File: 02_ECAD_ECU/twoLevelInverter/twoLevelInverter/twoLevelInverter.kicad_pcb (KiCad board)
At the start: 2 copper layers, 88.9 x 115.3 mm, 72 parts, among them IC1 MP9486AGN-Z, IC2 INA240A4DR, IC3 BTN8982TAAUMA1, IC4 INA240A4DR, IC5 BTN8982TAAUMA1, IC6 INA240A4DR, IC7 BTN8982TAAUMA1, J1 FX10A-80S_8-SV_71_, J2 43045-0812, J3 Screw_Terminal_01x04, J4 Screw_Terminal_01x04, J5 Screw_Terminal_01x02, J6 Screw_Terminal_01x02, J7 Screw_Terminal_01x02, U1 290mA, U10 30k, U11 2.4k, U12 22u, U13 15u, U14 RED, U15 1k, U2 100k, U3 68k, U4 MP2303ADN-LF, U5 10nF, U6 100nF, U7 3.3nF, U8 5.6k, U9 10k

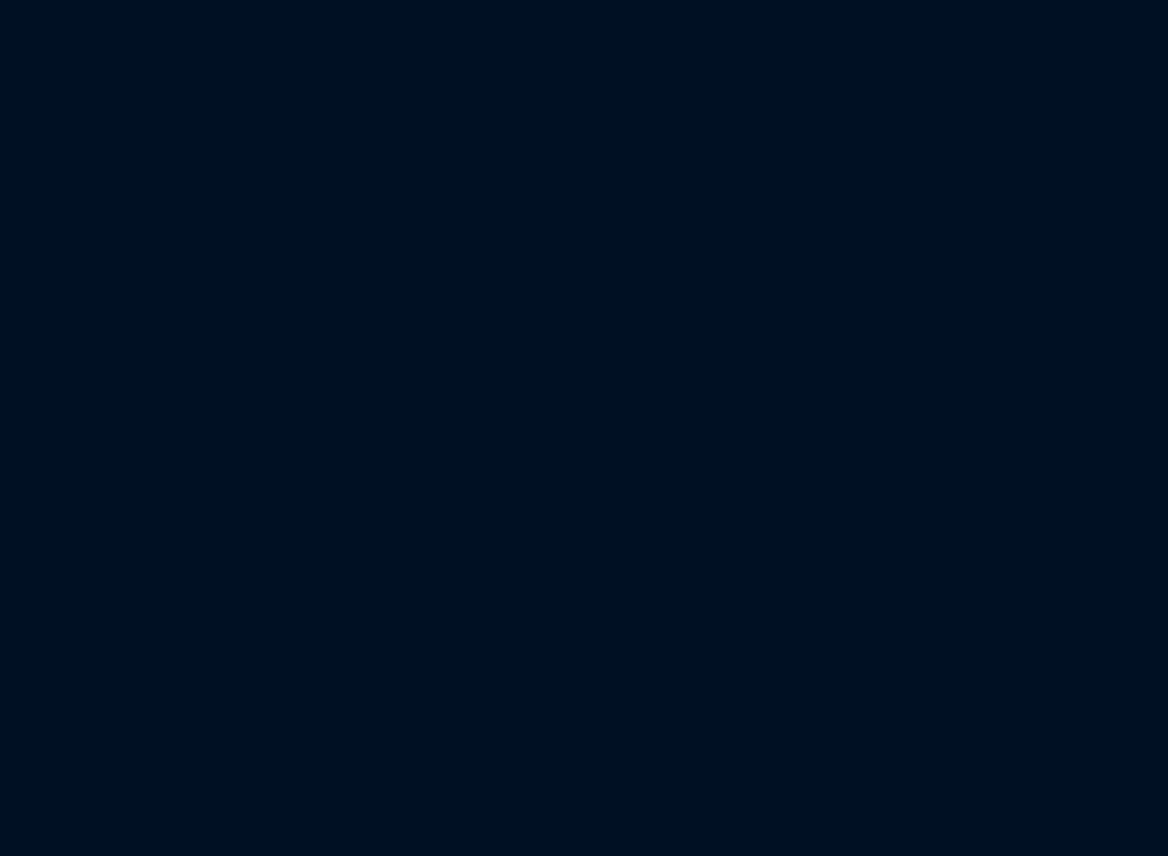
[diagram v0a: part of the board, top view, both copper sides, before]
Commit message: encoder, pwm, hall signals mapped
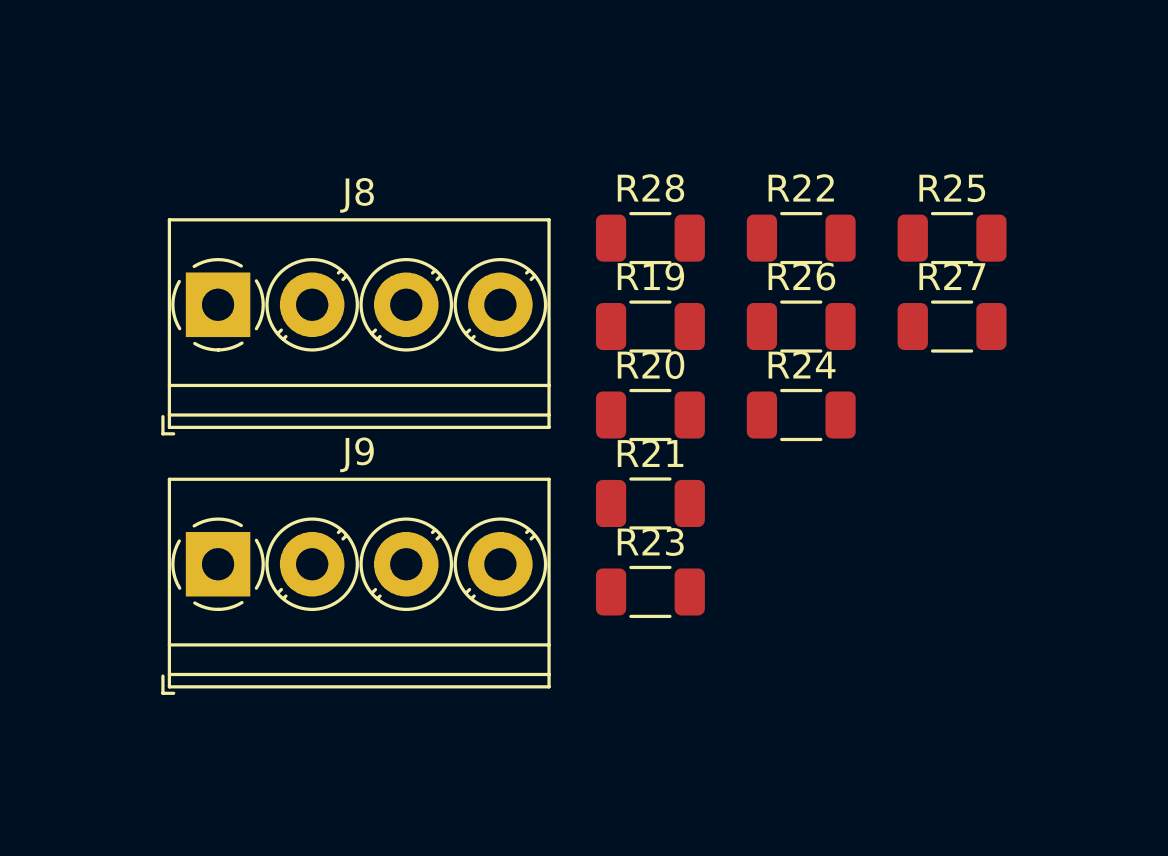
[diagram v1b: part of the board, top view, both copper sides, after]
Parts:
- added J8: Screw_Terminal_01x04, TerminalBlock_Phoenix:TerminalBlock_Phoenix_PT-1,5-4-3.5-H_1x04_P3.50mm_Horizontal, F.Cu at (103.6, 84.3)
- added J9: Screw_Terminal_01x04, TerminalBlock_Phoenix:TerminalBlock_Phoenix_PT-1,5-4-3.5-H_1x04_P3.50mm_Horizontal, F.Cu at (103.6, 94.0)
- added R19: 1k, Resistor_SMD:R_1206_3216Metric, F.Cu at (119.7, 85.1)
- added R20: 1k5, Resistor_SMD:R_1206_3216Metric, F.Cu at (119.7, 88.4)
- added R21: 1k, Resistor_SMD:R_1206_3216Metric, F.Cu at (119.7, 91.7)
- added R22: 1k5, Resistor_SMD:R_1206_3216Metric, F.Cu at (125.3, 81.8)
- added R23: 1k, Resistor_SMD:R_1206_3216Metric, F.Cu at (119.7, 95.0)
- added R24: 1k5, Resistor_SMD:R_1206_3216Metric, F.Cu at (125.3, 88.4)
- added R25: 1k, Resistor_SMD:R_1206_3216Metric, F.Cu at (130.9, 81.8)
- added R26: 1k5, Resistor_SMD:R_1206_3216Metric, F.Cu at (125.3, 85.1)
- added R27: 1k, Resistor_SMD:R_1206_3216Metric, F.Cu at (130.9, 85.1)
- added R28: 1k5, Resistor_SMD:R_1206_3216Metric, F.Cu at (119.7, 81.8)
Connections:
- H1 pad 1: unconnected-(H1-Pad1) -> GND
- H2 pad 1: unconnected-(H2-Pad1) -> GND
- H3 pad 1: unconnected-(H3-Pad1) -> GND
- H4 pad 1: unconnected-(H4-Pad1) -> GND
- IC2 pad 5: /driver/OU1_shunt -> /current_A
- IC4 pad 5: /driver/OU2_shunt -> /current_B
- IC6 pad 5: /driver/OU3_shunt -> /current_C
- J1 pad 21: unconnected-(J1-Pad21) -> /current_A
- J1 pad 25: unconnected-(J1-Pad25) -> /A_1_3V3
- J1 pad 27: unconnected-(J1-Pad27) -> /B_1_3V3
- J1 pad 29: unconnected-(J1-Pad29) -> /HB3_IN
- J1 pad 33: unconnected-(J1-Pad33) -> /HB2_IN
- J1 pad 37: unconnected-(J1-Pad37) -> /HALL_B_3V3
- J1 pad 39: unconnected-(J1-Pad39) -> /current_C
- J1 pad 43: unconnected-(J1-Pad43) -> /HALL_A_3V3
- J1 pad 45: unconnected-(J1-Pad45) -> /current_B
- J1 pad 49: unconnected-(J1-Pad49) -> /HALL_C_3V3
- J1 pad 51: unconnected-(J1-Pad51) -> /HB1_IN
- J4 pad 1: /B_2 -> /Phase_A
- J4 pad 2: /A_2 -> /Phase_B
- J4 pad 3: GND -> /Phase_C
- J4 pad 4: +5V -> unconnected-(J4-Pad4)
- R10 pad 1: /driver/HB2_IN -> /HB2_IN
- R15 pad 1: /driver/HB3_IN -> /HB3_IN
- R5 pad 1: /driver/HB1_IN -> /HB1_IN

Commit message: V1.0  not reviewed
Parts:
- removed FB1: 600 @ 600MHz, Inductor_SMD:L_1206_3216Metric
- removed J6, J7: Screw_Terminal_01x02, TerminalBlock_Phoenix:TerminalBlock_Phoenix_PT-1,5-2-5.0-H_1x02_P5.00mm_Horizontal
- removed J9: Screw_Terminal_01x04, TerminalBlock_Phoenix:TerminalBlock_Phoenix_PT-1,5-4-3.5-H_1x04_P3.50mm_Horizontal
- removed U10: 30k, Resistor_SMD:R_0805_2012Metric
- removed U11: 2.4k, Resistor_SMD:R_0603_1608Metric
- removed U12: 22u, Capacitor_SMD:C_0805_2012Metric
- removed U13: 15u, max_KiCAD_lib:LVS505020-150M-N
- removed U3: 68k, Resistor_SMD:R_0805_2012Metric
- removed U4: MP2303ADN-LF, max_KiCAD_lib:SOIC127P600X170-9N
- removed U5: 10nF, Capacitor_SMD:C_0805_2012Metric
- removed U6: 100nF, Capacitor_SMD:C_0603_1608Metric
- removed U7: 3.3nF, Capacitor_SMD:C_0603_1608Metric
- removed U8: 5.6k, Resistor_SMD:R_0603_1608Metric
- removed U9: 10k, Resistor_SMD:R_1206_3216Metric
- added C18: 100uF, max_KiCAD_lib:100uF_wuerth, F.Cu at (206.9, 73.9)
- added C19: 68 uF, max_KiCAD_lib:68uFcap, F.Cu at (218.4, 74.2)
- added D3: D_Schottky, max_KiCAD_lib:schottydiode50V, F.Cu at (207.3, 85.0)
- added IC8: LM2675N-3.3_NOPB, max_KiCAD_lib:LM2675N, F.Cu at (214.4, 83.8)
- added L2: 47uH, Capacitor_SMD:C_0805_2012Metric, F.Cu at (214.6, 93.7)
- C17: value 10uF/24V -> 10 nF
- D1: value LED_Small -> 24V
- J3, J4, J8: footprint TerminalBlock_Phoenix:TerminalBlock_Phoenix_PT-1,5-4-3.5-H_1x04_P3.50mm_Horizontal -> max_KiCAD_lib:screwconnector_4_wuerth
- J5: value Screw_Terminal_01x02 -> Screw_Terminal_01x04; footprint TerminalBlock_Phoenix:TerminalBlock_Phoenix_PT-1,5-2-5.0-H_1x02_P5.00mm_Horizontal -> max_KiCAD_lib:screwconnector_4_wuerth
- U1: value 290mA -> 5V; footprint Fuse:Fuse_1206_3216Metric -> LED_SMD:LED_1206_3216Metric
- U14: value RED -> 3V3; footprint LED_SMD:LED_0603_1608Metric -> LED_SMD:LED_1206_3216Metric
- U2: value 100k -> 1k
- moved J8 140.5 mm to (231.6, 142.2), turned to 90 degrees
- moved C7 139.4 mm to (206.2, 125.7), turned to -90 degrees
- moved D1 138.8 mm to (225.0, 56.5), turned to 180 degrees
- moved R1 133.6 mm to (220.0, 56.5), turned to 0 degrees
- moved R16 130.7 mm to (197.5, 125.6), turned to 90 degrees
- moved R14 120.6 mm to (204.0, 96.6), turned to -90 degrees
- moved R15 119.7 mm to (206.5, 96.6), turned to -90 degrees
- moved C10 119.0 mm to (198.9, 96.6), turned to -90 degrees
- moved C8 117.8 mm to (196.3, 96.6), turned to -90 degrees
- moved R28 113.5 mm to (224.8, 124.8), turned to -90 degrees
- moved R21 112.3 mm to (231.7, 100.6), turned to 180 degrees
- moved R26 108.5 mm to (231.7, 106.7)
- moved R22 107.6 mm to (231.7, 98.0)
- moved C4 106.9 mm to (185.7, 125.4), turned to -90 degrees
- moved J4 105.6 mm to (163.8, 154.2), turned to 0 degrees
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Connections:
- C1 pad 1: GND -> +3V3
- C1 pad 2: +3V3 -> GND
- C17 pad 1: /step-down converter 3.3V/IN -> Net-(C17-Pad1)
- C17 pad 2: GND -> Net-(C17-Pad2)
- C2 pad 2: /driver/HB1_IS -> /HB1_IS
- C4 pad 1: GND -> +3V3
- C4 pad 2: +3V3 -> GND
- C5 pad 2: /driver/HB2_IS -> /HB2_IS
- C7 pad 1: GND -> +3V3
- C7 pad 2: +3V3 -> GND
- C8 pad 2: /driver/HB3_IS -> /HB3_IS
- IC1 pad 6: /step-down converter_5V/En -> /EN_5V
- IC1 pad 7: /step-down converter_5V/En -> /EN_5V
- IC1 pad 9: unconnected-(IC1-Pad9) -> GND
- IC2 pad 3: +3V3 -> GND
- IC2 pad 7: GND -> +3V3
- IC3 pad 4: /driver/HB1_OUT -> unconnected-(IC3-Pad4)
- IC3 pad 6: /driver/HB1_IS -> /HB1_IS
- IC4 pad 3: +3V3 -> GND
- IC4 pad 7: GND -> +3V3
- IC5 pad 4: /driver/HB2_OUT -> unconnected-(IC5-Pad4)
- IC5 pad 6: /driver/HB2_IS -> /HB2_IS
- IC6 pad 3: +3V3 -> GND
- IC6 pad 7: GND -> +3V3
- IC7 pad 4: /driver/HB3_OUT -> unconnected-(IC7-Pad4)
- IC7 pad 6: /driver/HB3_IS -> /HB3_IS
- J1 pad 15: unconnected-(J1-Pad15) -> /HB2_IS
- J1 pad 17: unconnected-(J1-Pad17) -> /HB3_IS
- J1 pad 21: /current_A -> /current_C
- J1 pad 37: /HALL_B_3V3 -> /HALL_C_3V3
- J1 pad 39: /current_C -> /current_B
- J1 pad 43: /HALL_A_3V3 -> /HALL_B_3V3
- J1 pad 45: /current_B -> /current_A
- J1 pad 49: /HALL_C_3V3 -> /HALL_A_3V3
- J1 pad 7: unconnected-(J1-Pad7) -> /HB1_IS
- J1 pad 73: unconnected-(J1-Pad73) -> /EN_5V
- J1 pad 75: unconnected-(J1-Pad75) -> /HB3_INH
- J1 pad 77: unconnected-(J1-Pad77) -> /HB2_INH
- J1 pad 79: unconnected-(J1-Pad79) -> /HB1_INH
- J4 pad 4: unconnected-(J4-Pad4) -> GND
- J5 pad 1: GND -> +5V
- J5 pad 2: +24V -> +3V3
- J8 pad 4: unconnected-(J8-Pad4) -> +5V
- R12 pad 2: /driver/HB3_IS -> /HB3_IS
- R14 pad 1: /driver/HB3_INH -> /HB3_INH
- R2 pad 2: /driver/HB1_IS -> /HB1_IS
- R4 pad 1: /driver/HB1_INH -> /HB1_INH
- R7 pad 2: /driver/HB2_IS -> /HB2_IS
- R9 pad 1: /driver/HB2_INH -> /HB2_INH
- U1 pad 1: Net-(FB1-Pad1) -> Net-(U1-Pad1)
- U2 pad 1: /step-down converter 3.3V/IN -> Net-(U1-Pad1)
- U2 pad 2: /step-down converter 3.3V/EN -> GND
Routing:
- net +5V: track 0.00 -> 218.8 mm
- net +3V3: track 0.00 -> 152.3 mm, vias 0 -> 4
- net /HALL_C_3V3: track 0.00 -> 107.1 mm, vias 0 -> 2
- net /current_C: track 0.00 -> 102.9 mm, vias 0 -> 2
- net /HALL_B_3V3: track 0.00 -> 100.1 mm, vias 0 -> 2
- net /HALL_A_3V3: track 0.00 -> 92.9 mm, vias 0 -> 2
- net /B_1_3V3: track 0.00 -> 91.4 mm, vias 0 -> 2
- net /A_1_3V3: track 0.00 -> 89.1 mm, vias 0 -> 2
- net /current_B: track 0.00 -> 80.1 mm, vias 0 -> 2
- net /EN_5V: track 0.00 -> 65.0 mm, vias 0 -> 2
- net /HB3_IS: track 0.00 -> 63.8 mm, vias 0 -> 2
- net /HB3_IN: track 0.00 -> 61.2 mm
- net /current_A: track 0.00 -> 60.2 mm, vias 0 -> 2
- net GND: track 0.00 -> 56.8 mm, vias 0 -> 86
- net /HB3_INH: track 0.00 -> 54.0 mm, vias 0 -> 2
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- added copper zone on F.Cu, net +24V
- added copper zone on In2.Cu, net +24V
- added copper zone on F.Cu, net +3V3
- added copper zone on F.Cu, net +5V
- added copper zone on F.Cu, net /Phase_A
- added copper zone on In2.Cu, net /Phase_A
- added copper zone on F.Cu, net /Phase_B
- added copper zone on In2.Cu, net /Phase_B
- added copper zone on F.Cu, net /Phase_C
- added copper zone on In2.Cu, net /Phase_C
- added copper zone on F.Cu, net /driver/HB1_OUT
- added copper zone on F.Cu, net /driver/HB2_OUT
- added copper zone on F.Cu, net /driver/HB3_OUT
- added copper zone on B.Cu, net GND
- added copper zone on F.Cu, net GND
- added copper zone on In1.Cu, net GND
- added copper zone on F.Cu, net Net-(C13-Pad2)
- added copper zone on F.Cu, net Net-(C17-Pad1)
- added copper zone on F.Cu, net Net-(C17-Pad2)
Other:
- board size 88.9 x 115.3 mm -> 101.6 x 120.4 mm
- copper layers 2 -> 4
- board text added: "+"
- board text added: "24V GND 3V3 5V"
- board text added: "B_1 A_1 GND 5V"
- board text added: "HALL_A HALL_B HALL_C 5V"
- board text added: "Phase A"
- board text added: "Phase A Phase B Phase C GND"
- board text added: "Phase B"
- board text added: "Phase C"
- board text added: "_"

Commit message: orderd, added gerber files
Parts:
- added G***: LOGO, LOGO, F.Cu at (240.5, 89.7)
- D1, U1, U14: footprint LED_SMD:LED_1206_3216Metric -> LED_SMD:LED_0805_2012Metric
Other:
- board text added: "1"
- board text added: "Tellur V1.0 @Max"
